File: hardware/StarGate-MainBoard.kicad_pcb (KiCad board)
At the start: 4 copper layers, 146.1 x 55 mm, 168 parts, among them IC1 TB6612FNG, IC2 TB6612FNG, IC3 TB6612FNG, IC4 TB6612FNG, IC5 TB6612FNG, IC6 TB6612FNG, IC7 SGTL5000, J1 PJ-037A, J10 Conn_01x02_Pin, J11 Conn_01x03_Male, J12 Conn_01x02_Pin, J13 Conn_01x02_Pin, J14 Conn_01x02_Pin, J15 Conn_01x02_Pin, J16 Conn_01x02_Pin, J17 Conn_01x02_Pin, J18 Conn_01x02_Pin, J19 Conn_01x02_Pin, J2 Conn_01x03_Socket, J20 Conn_01x02_Pin, J21 Conn_01x02_Pin, J22 Conn_01x02_Pin, J23 Conn_01x02_Pin, J24 Conn_01x03_Socket, J26 Micro_SD_Card_Det, J27 Conn_01x03_Male, J28 Conn_01x02_Pin, J29 Conn_01x02_Pin, J3 Conn_01x02_Pin, J30 Conn_01x02_Pin, J31 Conn_01x02_Pin, J32 Conn_01x03_Male, J33 Conn_01x02_Pin, J34 USB_C_Receptacle, J4 Conn_01x04_Pin, J5 Conn_01x02_Pin, J6 Conn_01x02_Pin, J7 Conn_01x02_Pin, J8 Conn_01x02_Pin, J9 Conn_01x02_Pin, Q1 FDN340P, Q12 PMOS, Q2 FDN337N, Q3 N0400P-ZK-E1-AY, SW1 SW_Push_Dual, SW2 SW_Push_Dual, U1 SN74LVC1T45DBV, U10 AZ1084-1.8, U11 USBLC6-4SC6, U12 STMPS2151STR, U2 PCA9685, U3 PCA9685, U4 PCA9685, U5 FM6124, U6 ESP32-S3-WROOM-1-N16R2, U7 MC33063ADR, U8 TPA6017A2, U9 RT6219, X1 SG-210SDF (11.2896MHz)

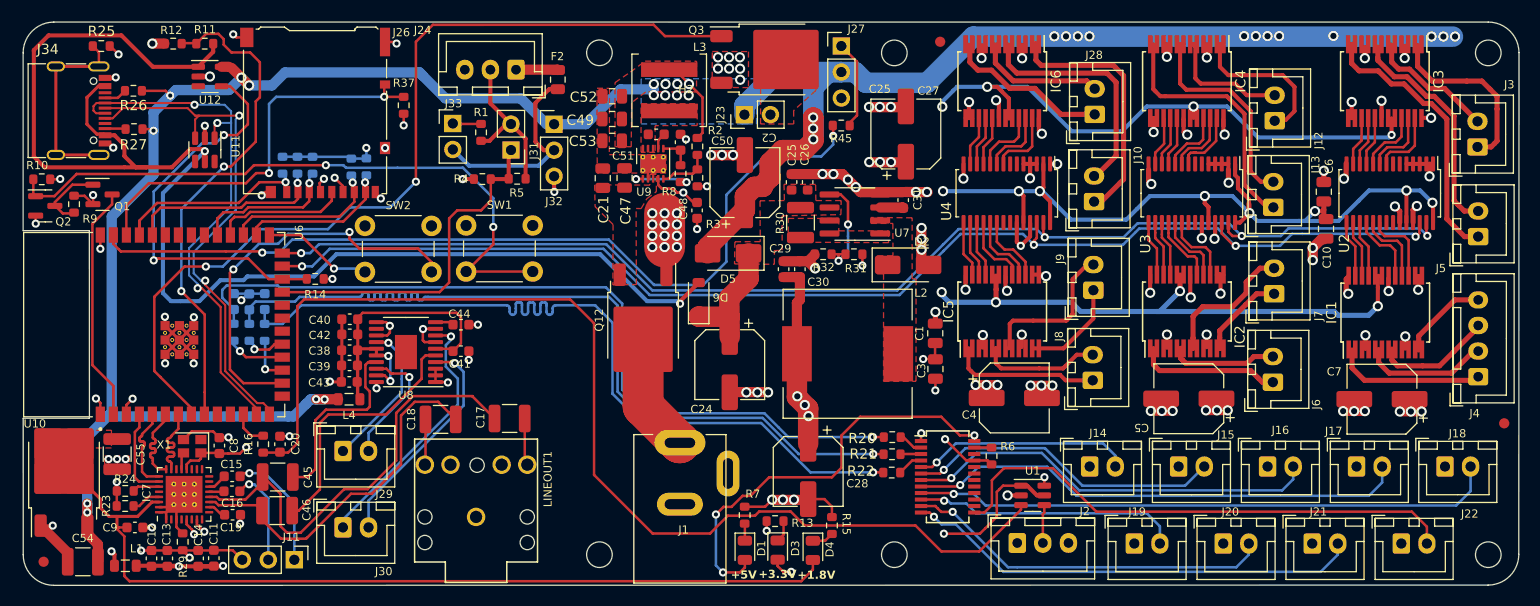
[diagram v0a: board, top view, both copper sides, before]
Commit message: Added JTAG Port
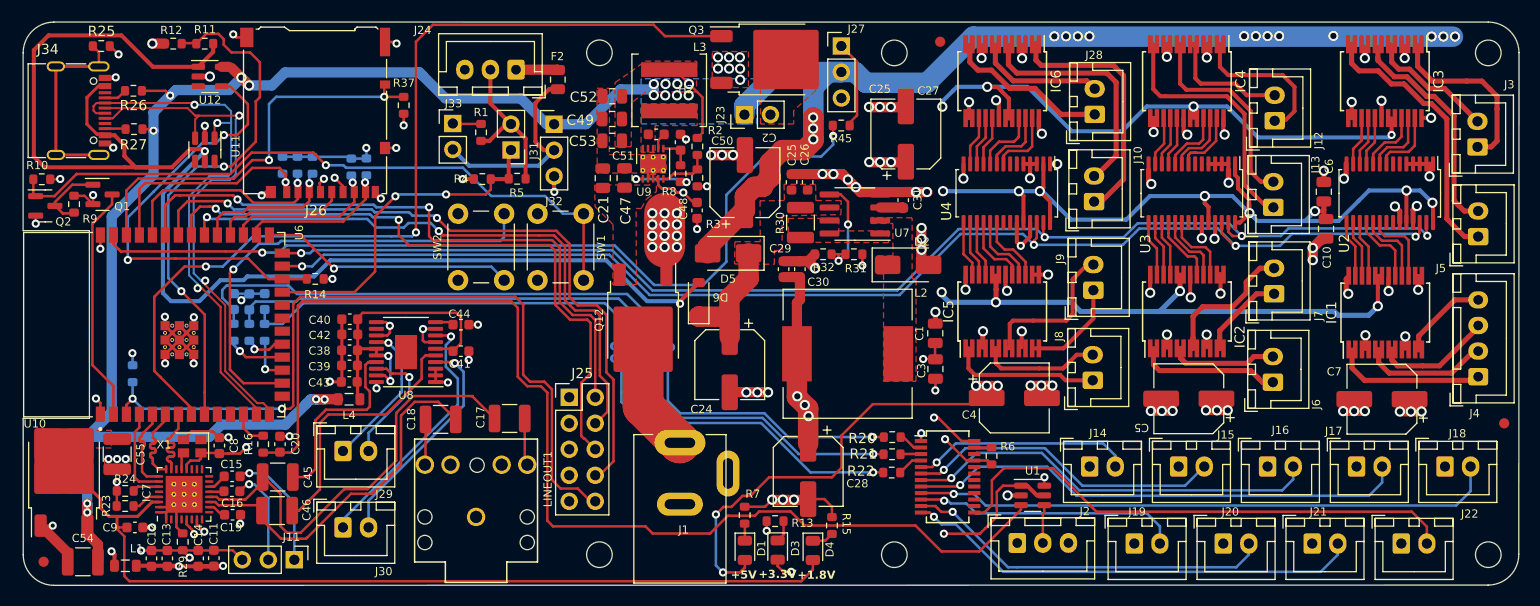
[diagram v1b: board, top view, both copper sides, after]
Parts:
- added J25: Conn_02x05_Odd_Even, Connector_PinHeader_2.54mm:PinHeader_2x05_P2.54mm_Vertical, F.Cu at (98.8, 80.9)
- added R28: 10k, Resistor_SMD:R_0603_1608Metric, B.Cu at (56.2, 78.6)
- J26: footprint Connector_Card:microSD_HC_Hirose_DM3AT-SF-PEJM5 -> PLH:microSD_HC_Hirose_DM3AT-SF-PEJM5
- moved SW2 10.5 mm to (88.0, 69.4), turned to 90 degrees
- moved SW1 8.79 mm to (95.7, 69.4), turned to 90 degrees
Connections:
- U5 pad 24: +5V -> +3V3
- U6 pad 3: +3V3 -> /nRESET
- U6 pad 32: unconnected-(U6-IO39-Pad32) -> /MTCK
- U6 pad 33: unconnected-(U6-IO40-Pad33) -> /MTDO
- U6 pad 34: unconnected-(U6-IO41-Pad34) -> /MTDI
- U6 pad 35: unconnected-(U6-IO42-Pad35) -> /MTMS
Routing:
- net /nRESET: track 0.00 -> 76.8 mm, vias 0 -> 2
- net /MTDI: track 0.00 -> 69.2 mm, vias 0 -> 2
- net /MTDO: track 0.00 -> 63.3 mm, vias 0 -> 2
- net /MTMS: track 0.00 -> 62.7 mm, vias 0 -> 2
- net /MTCK: track 0.00 -> 59.0 mm, vias 0 -> 2
- net /BOOT_MODE_A: track 10.8 -> 24.9 mm
- net /BOOT_MODE_B: track 39.0 -> 45.6 mm, vias 2 -> 1
- net +3V3: track 270.7 -> 275.0 mm, vias 37 -> 38
- net +5V: track 313.8 -> 317.4 mm, vias 56 -> 55
- net /USB_VBUS_EN: track 39.8 -> 43.3 mm
- net /LED_PWM: track 87.8 -> 90.7 mm
- net /NEO_MOSI: track 110.8 -> 113.4 mm
- net /USB_VBUS_DET: track 48.4 -> 50.9 mm
- net Net-(Q2-G): track 63.8 -> 66.0 mm, vias 2 -> 1
- net /SD_D2: track 19.5 -> 21.7 mm
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
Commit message: Added CAP to reset line
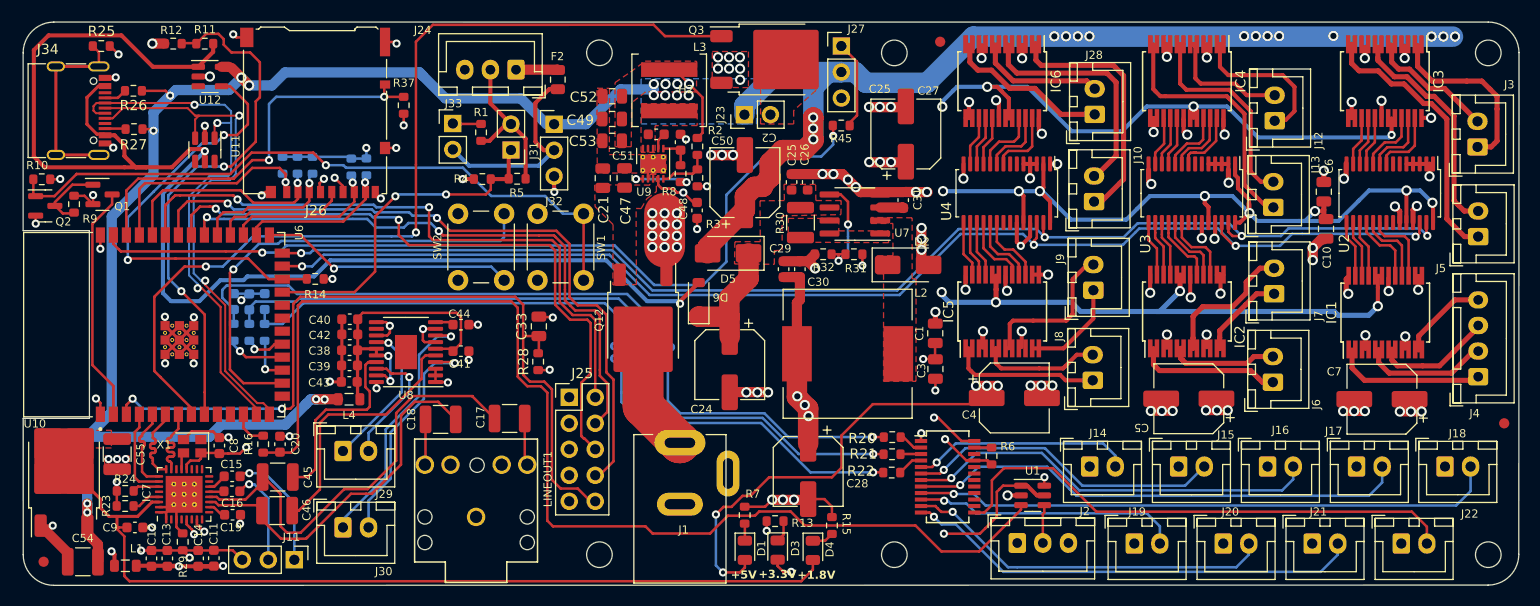
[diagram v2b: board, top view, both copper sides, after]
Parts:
- added C33: 0.1uF, Capacitor_SMD:C_0805_2012Metric, F.Cu at (95.8, 73.9)
- R28: moved to F.Cu
- moved R28 39.6 mm to (95.8, 77.4), turned to 90 degrees
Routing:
- net /nRESET: track 76.8 -> 78.4 mm
- net GND: track 189.2 -> 190.5 mm, vias 121 -> 122
